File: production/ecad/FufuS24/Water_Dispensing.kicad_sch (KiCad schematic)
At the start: 0 parts

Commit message: Water Sensing Added
Lots of global labels to symbolize wires going from 5V and GPIO to water sensor
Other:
- note added: "PUMP"
- note added: "WATER SENSING #1"
- note added: "WATER SENSING #2"

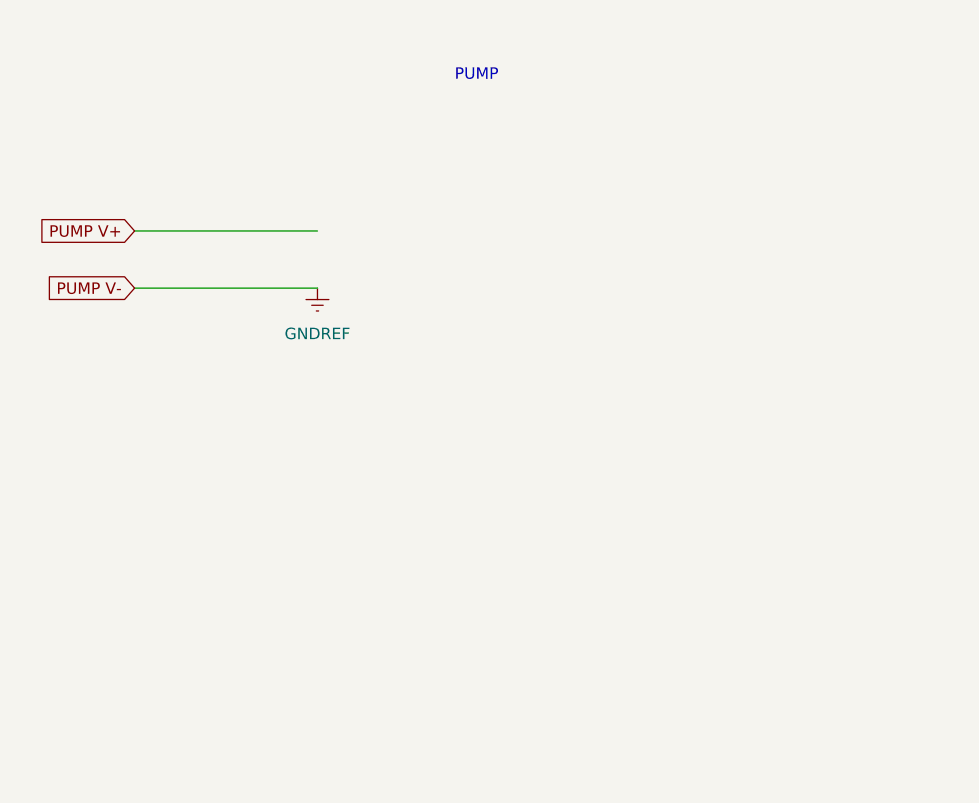
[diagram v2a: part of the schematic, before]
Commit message: Water Dispensing Draft1
Added Pump Control, Symbols for Schottkey diode (may need to change to smaller package), added text to show where gpio pins go
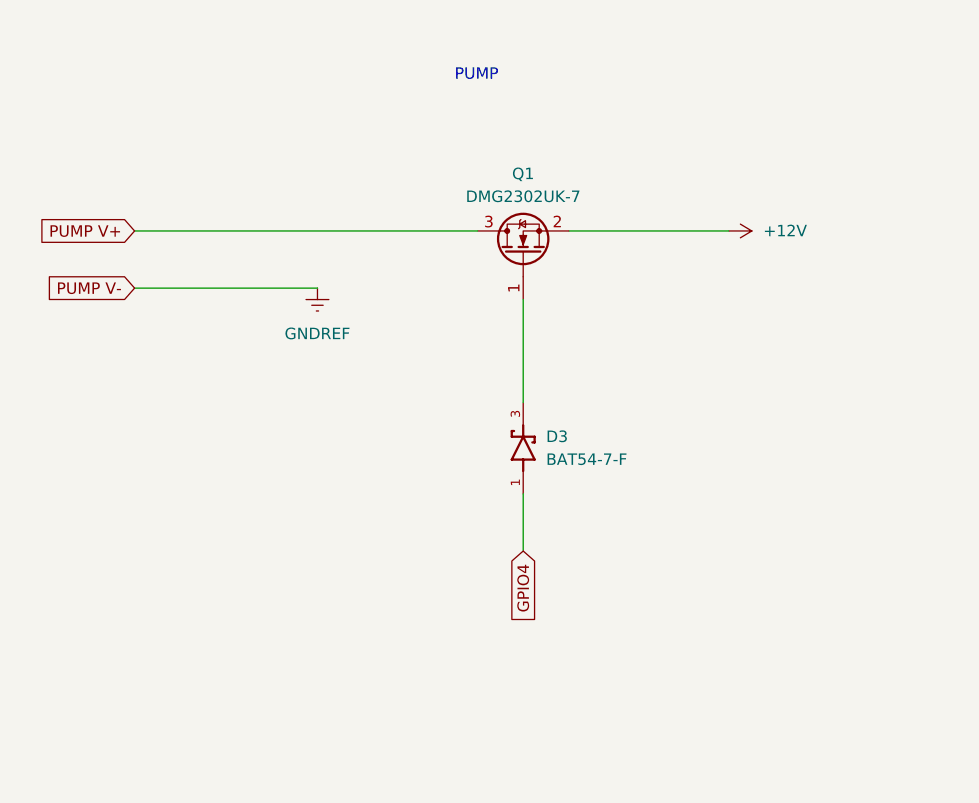
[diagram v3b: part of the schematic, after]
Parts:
- added D3: BAT54-7-F, footprints:SOT91P240X110-3N, symbol BAT54-7-F:BAT54-7-F
- added Q1: DMG2302UK-7, Package_TO_SOT_SMD:SOT-23, symbol Transistor_FET:DMG2302U
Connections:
- net PUMP V+: now also Q1.3 (D)
- new net: D3.3, Q1.1 (G)
- new net +12V: Q1.2 (S)
- new net GPIO4: D3.1
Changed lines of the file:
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@@
 (kicad_sch (version 20230121) (generator eeschema)
   (paper "A4")
+  (wire (pts (xy 67.31 41.91) (xy 67.31 53.34))
+    (stroke (width 0) (type default))
+  )
+  (wire (pts (xy 67.31 63.5) (xy 67.31 69.85))
+    (stroke (width 0) (type default))
+  )
   (wire (pts (xy 240.03 54.61) (xy 274.32 54.61))
     (stroke (width 0) (type default))
@@
     (stroke (width 0) (type default))
   )
-  (wire (pts (xy 24.13 34.29) (xy 44.45 34.29))
-    (stroke (width 0) (type default))
-  )
   (wire (pts (xy 240.03 62.23) (xy 274.32 62.23))
     (stroke (width 0) (type default))
@@
   )
   (polyline (pts (xy 128.27 10.16) (xy 128.27 100.33))
+    (stroke (width 0) (type default))
+  )
+  (wire (pts (xy 24.13 34.29) (xy 62.23 34.29))
+    (stroke (width 0) (type default))
+  )
+  (wire (pts (xy 72.39 34.29) (xy 90.17 34.29))
     (stroke (width 0) (type default))
   )
@@
     )
   )
+  (global_label "GPIO4" (shape input) (at 67.31 69.85 270) (fields_autoplaced)
+    (effects (font (size 1.27 1.27)) (justify right))
+    (property "Intersheetrefs" "${INTERSHEET_REFS}" (at 67.31 78.52 90)
+      (effects (font (size 1.27 1.27)) (justify right) hide)
+    )
+  )
   (global_label "WATERSENSOR2 GND" (shape input) (at 240.03 43.18 180) (fields_autoplaced)
     (effects (font (size 1.27 1.27)) (justify right))
@@
     (property "Intersheetrefs" "${INTERSHEET_REFS}" (at 217.8135 34.29 0)
       (effects (font (size 1.27 1.27)) (justify right) hide)
+    )
+  )
+  (symbol (lib_id "BAT54-7-F:BAT54-7-F") (at 67.31 58.42 90) (unit 1)
+    (in_bom yes) (on_board yes) (dnp no) (fields_autoplaced)
+    (property "Reference" "D3" (at 69.85 57.15 90)
+      (effects (font (size 1.27 1.27)) (justify right))
+    )
+    (property "Value" "BAT54-7-F" (at 69.85 59.69 90)
+      (effects (font (size 1.27 1.27)) (justify right))
+    )
+    (property "Footprint" "footprints:SOT91P240X110-3N" (at 67.31 58.42 0)
+      (effects (font (size 1.27 1.27)) (justify bottom) hide)
+    )
+    (property "Datasheet" "" (at 67.31 58.42 0)
+      (effects (font (size 1.27 1.27)) hide)
+    )
+    (property "MF" "Diodes Inc." (at 67.31 58.42 0)
+      (effects (font (size 1.27 1.27)) (justify bottom) hide)
+    )
+    (property "Description" "\nSchottky Diode 200mA 30V 0.32Vf SOT23 | Diodes Inc BAT54-7-F\n" (at 67.31 58.42 0)
+      (effects (font (size 1.27 1.27)) (justify bottom) hide)
+    )
+    (property "Package" "SOT-23 Diodes Inc." (at 67.31 58.42 0)
+      (effects (font (size 1.27 1.27)) (justify bottom) hide)
+    )
+    (property "Price" "None" (at 67.31 58.42 0)
+      (effects (font (size 1.27 1.27)) (justify bottom) hide)
+    )
+    (property "Check_prices" "https://www.snapeda.com/parts/BAT54-7-F/Diodes+Inc./view-part/?ref=eda" (at 67.31 58.42 0)
+      (effects (font (size 1.27 1.27)) (justify bottom) hide)
+    )
+    (property "STANDARD" "IPC-7351B" (at 67.31 58.42 0)
+      (effects (font (size 1.27 1.27)) (justify bottom) hide)
+    )
+    (property "PARTREV" "32-2" (at 67.31 58.42 0)
+      (effects (font (size 1.27 1.27)) (justify bottom) hide)
+    )
+    (property "SnapEDA_Link" "https://www.snapeda.com/parts/BAT54-7-F/Diodes+Inc./view-part/?ref=snap" (at 67.31 58.42 0)
+      (effects (font (size 1.27 1.27)) (justify bottom) hide)
+    )
+    (property "MP" "BAT54-7-F" (at 67.31 58.42 0)
+      (effects (font (size 1.27 1.27)) (justify bottom) hide)
+    )
+    (property "Purchase-URL" "https://www.snapeda.com/api/url_track_click_mouser/?unipart_id=78728&manufacturer=Diodes Inc.&part_name=BAT54-7-F&search_term=bat54-7-f" (at 67.31 58.42 0)
+      (effects (font (size 1.27 1.27)) (justify bottom) hide)
+    )
+    (property "Availability" "In Stock" (at 67.31 58.42 0)
+      (effects (font (size 1.27 1.27)) (justify bottom) hide)
+    )
+    (property "MANUFACTURER" "Diodes" (at 67.31 58.42 0)
+      (effects (font (size 1.27 1.27)) (justify bottom) hide)
+    )
+    (pin "1")
+    (pin "3")
+    (instances
+      (project "FufuS24"
+        (path "/c4c3980b-c8c0-435e-abdc-bbed2349d7ac/4167d6e6-5417-44cf-9a0c-baf8fab8b739"
+          (reference "D3") (unit 1)
+        )
+      )
+    )
+  )
+  (symbol (lib_id "Transistor_FET:DMG2302U") (at 67.31 36.83 90) (unit 1)
+    (in_bom yes) (on_board yes) (dnp no) (fields_autoplaced)
+    (property "Reference" "Q1" (at 67.31 27.94 90)
+      (effects (font (size 1.27 1.27)))
+    )
+    (property "Value" "DMG2302UK-7" (at 67.31 30.48 90)
+      (effects (font (size 1.27 1.27)))
+    )
+    (property "Footprint" "Package_TO_SOT_SMD:SOT-23" (at 69.215 31.75 0)
+      (effects (font (size 1.27 1.27) italic) (justify left) hide)
+    )
+    (property "Datasheet" "http://www.diodes.com/assets/Datasheets/DMG2302U.pdf" (at 67.31 36.83 0)
+      (effects (font (size 1.27 1.27)) (justify left) hide)
+    )
+    (pin "1")
+    (pin "2")
+    (pin "3")
+    (instances
+      (project "FufuS24"
+        (path "/c4c3980b-c8c0-435e-abdc-bbed2349d7ac/4167d6e6-5417-44cf-9a0c-baf8fab8b739"
+          (reference "Q1") (unit 1)
+        )
+      )
     )
   )
@@
         )
       )
+    )
+  )
+  (symbol (lib_id "power:+12V") (at 90.17 34.29 270) (unit 1)
+    (in_bom yes) (on_board yes) (dnp no) (fields_autoplaced)
+    (property "Reference" "#PWR063" (at 86.36 34.29 0)
+      (effects (font (size 1.27 1.27)) hide)
+    )
+    (property "Value" "+12V" (at 93.98 34.29 90)
+      (effects (font (size 1.27 1.27)) (justify left))
+    )
+    (property "Footprint" "" (at 90.17 34.29 0)
+      (effects (font (size 1.27 1.27)) hide)
+    )
+    (property "Datasheet" "" (at 90.17 34.29 0)
+      (effects (font (size 1.27 1.27)) hide)
+    )
+    (pin "1")
+    (instances
+      (project "FufuS24"
+        (path "/c4c3980b-c8c0-435e-abdc-bbed2349d7ac/4167d6e6-5417-44cf-9a0c-baf8fab8b739"
+          (reference "#PWR063") (unit 1)
+        )
+      )

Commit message: Update Water_Dispensing.kicad_sch
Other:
- note added: "(Global Labels used in place of connectors for now)"
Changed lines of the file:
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@@
+    (effects (font (size 1.27 1.27)) (justify left bottom))
+  )
+  (text "(Global Labels used in place of connectors for now)"
+    (at 44.45 87.63 0)
+    (effects (font (size 1.27 1.27)) (justify left bottom))
+  )
+  (text "(Global Labels used in place of connectors for now)"
+    (at 220.98 78.74 0)
     (effects (font (size 1.27 1.27)) (justify left bottom))
   )
@@
     (effects (font (size 1.27 1.27)) (justify left bottom))
   )
+  (text "(Global Labels used in place of connectors for now)"
+    (at 144.78 77.47 0)
+    (effects (font (size 1.27 1.27)) (justify left bottom))
+  )

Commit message: removed diode, replaced with gate resistor
i like dinosaurs
transistor already had gate protection
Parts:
- removed D3: BAT54-7-F, footprints:SOT91P240X110-3N, symbol BAT54-7-F:BAT54-7-F
- added R20: 100, symbol Device:R_US
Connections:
- net +12V: no longer Q1.2 (S)
- net GNDREF: now also Q1.2 (S)
- net GPIO4: now also R20.2
- net at Q1.1 (G): now also R20.1
- net PUMP V+ renamed PUMP V-
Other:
- note added: "DIGITAL"

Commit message: Design review changes
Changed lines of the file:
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@@
     (stroke (width 0) (type default))
+  )
+  (text_box "Clarify Mode pin operation. Potentially reduce GPIO use"
+    (at 194.31 119.38 0) (size 21.59 12.7)
+    (stroke (width 0) (type default))
+    (fill (type none))
+    (effects (font (size 1.27 1.27)) (justify left top))
   )
   (text "DIGITAL" (at 275.59 66.04 0)

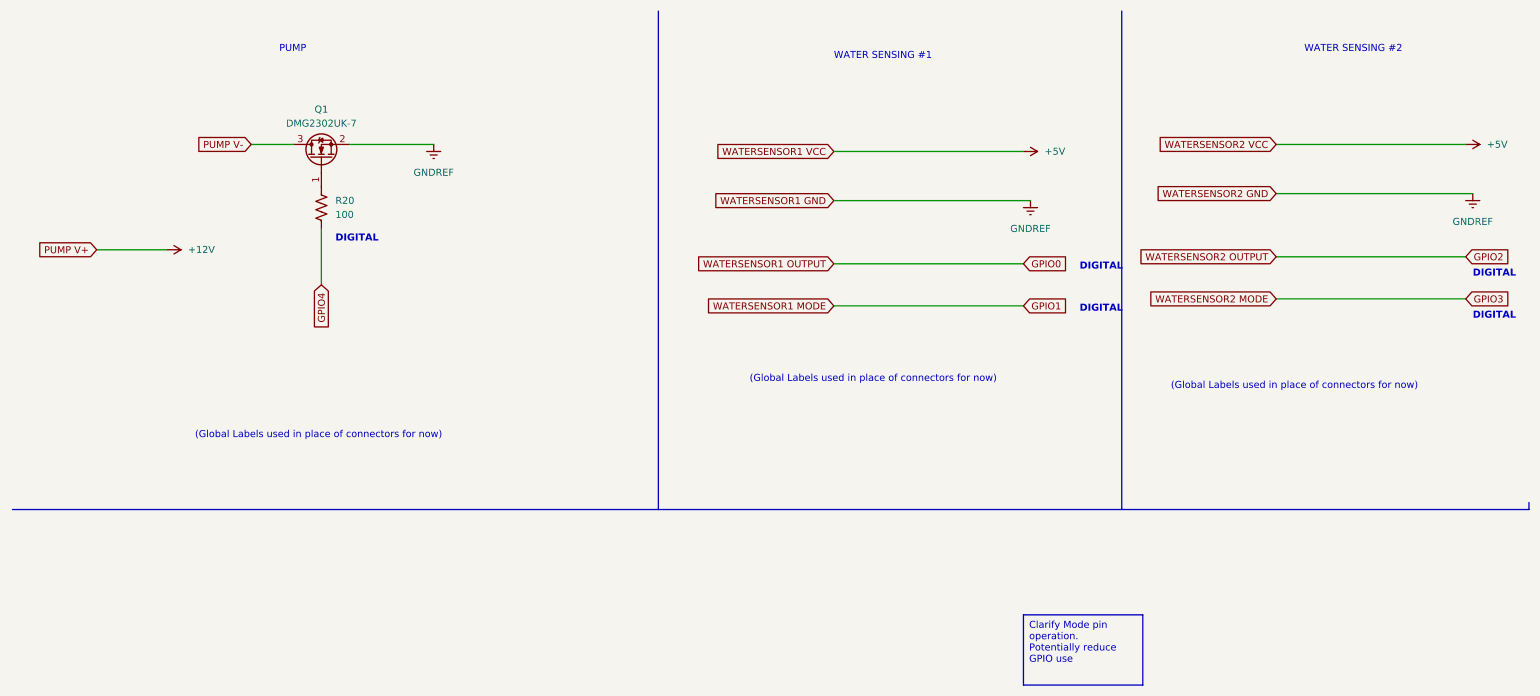
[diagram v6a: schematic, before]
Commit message: changed global label names water
what the summary said
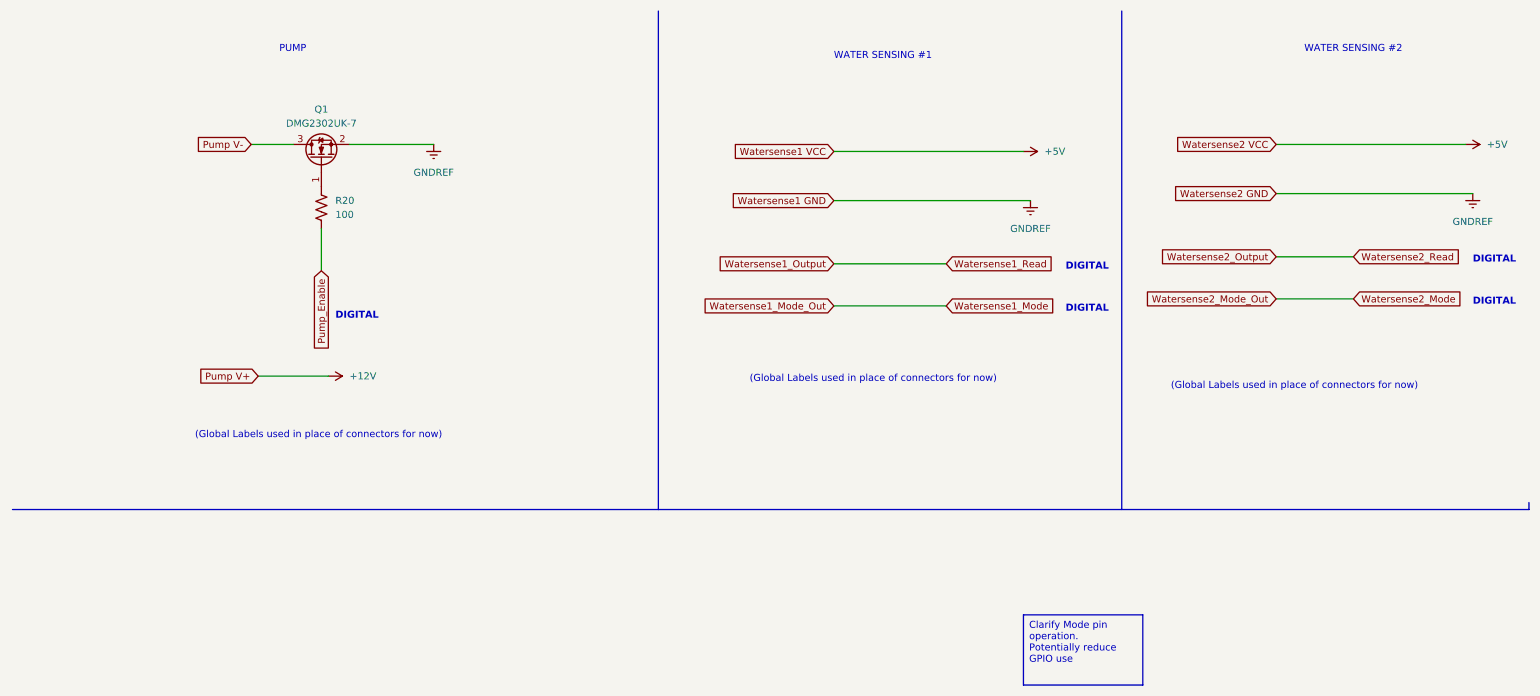
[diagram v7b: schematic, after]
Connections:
- net GPIO4 renamed Pump_Enable
- net PUMP V- renamed Pump V-
